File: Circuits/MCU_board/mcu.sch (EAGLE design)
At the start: 72 parts, among them IC1 RP111N331B-TR-FE, IC2 FT230XS, U1 TCA9548APWR, U2 USBLC6-2P6, U4 LSM9DS1, U5 STM32L452RECT6

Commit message: Finished first draft routing
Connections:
- net N$1 renamed D+
- net N$2 renamed D-
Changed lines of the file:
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@@
 </segment>
 </net>
-<net name="N$1" class="0">
+<net name="D+" class="0">
 <segment>
 <pinref part="CN1" gate="G$1" pin="D+"/>
@@
 <pinref part="U2" gate="G$1" pin="I/O1_2"/>
 <wire x1="205.74" y1="68.58" x2="195.58" y2="68.58" width="0.1524" layer="91"/>
+<label x="203.2" y="68.58" size="1.778" layer="95"/>
 </segment>
 </net>
-<net name="N$2" class="0">
+<net name="D-" class="0">
 <segment>
 <pinref part="CN1" gate="G$1" pin="D-"/>
@@
 <pinref part="U2" gate="G$1" pin="I/O2_2"/>
 <wire x1="205.74" y1="58.42" x2="195.58" y2="58.42" width="0.1524" layer="91"/>
+<label x="203.2" y="58.42" size="1.778" layer="95"/>
 </segment>
 </net>

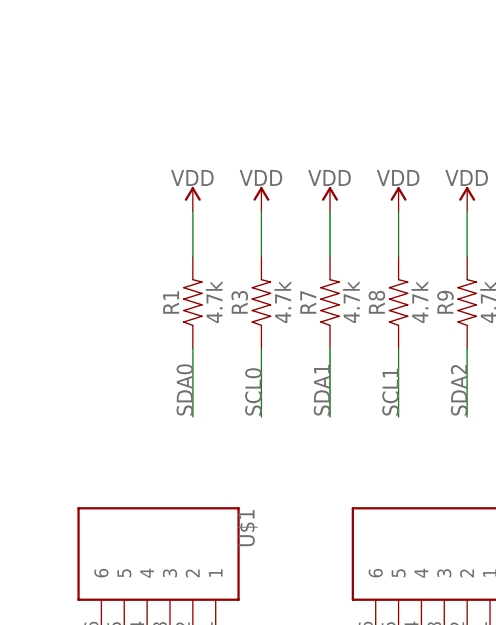
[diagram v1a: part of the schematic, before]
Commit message: Add pullups for MCU I2C lines
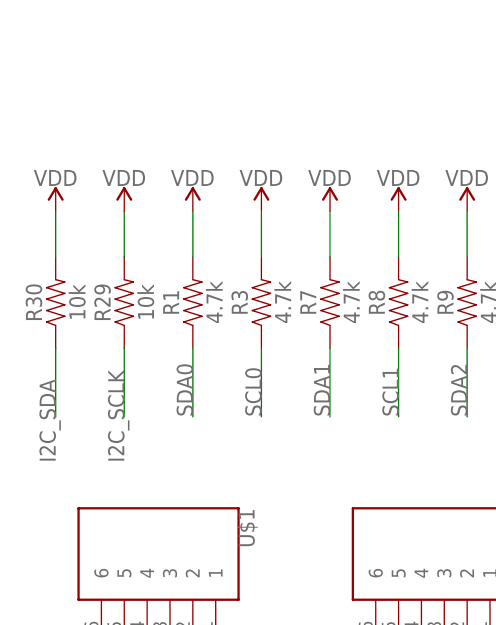
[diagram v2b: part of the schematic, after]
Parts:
- added R29, R30: 10k, SparkFun-Resistors:10KOHM-0603-1/10W-1%
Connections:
- net I2C_SCLK: now also R29.1
- net I2C_SDA: now also R30.1
- net VDD: now also R29.2, R30.2
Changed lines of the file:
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@@
 <?xml version="1.0" encoding="utf-8"?>
 <!DOCTYPE eagle SYSTEM "eagle.dtd">
-<eagle version="9.4.2">
+<eagle version="9.3.2">
 <drawing>
 <settings>
@@
 <part name="R25" library="SparkFun-Resistors" deviceset="10KOHM" device="-0603-1/10W-1%" value="10k"/>
 <part name="R26" library="SparkFun-Resistors" deviceset="10KOHM" device="-0603-1/10W-1%" value="10k"/>
+<part name="R29" library="SparkFun-Resistors" deviceset="10KOHM" device="-0603-1/10W-1%" value="10k"/>
+<part name="R30" library="SparkFun-Resistors" deviceset="10KOHM" device="-0603-1/10W-1%" value="10k"/>
+<part name="SUPPLY26" library="SparkFun-PowerSymbols" deviceset="VDD" device=""/>
+<part name="SUPPLY27" library="SparkFun-PowerSymbols" deviceset="VDD" device=""/>
 </parts>
 <sheets>
@@
 <attribute name="NAME" x="105.156" y="7.62" size="1.778" layer="95" font="vector" rot="R90" align="bottom-center"/>
 <attribute name="VALUE" x="108.204" y="7.62" size="1.778" layer="96" font="vector" rot="R90" align="top-center"/>
+</instance>
+<instance part="R29" gate="G$1" x="-215.9" y="119.38" smashed="yes" rot="R90">
+<attribute name="NAME" x="-217.424" y="119.38" size="1.778" layer="95" font="vector" rot="R90" align="bottom-center"/>
+<attribute name="VALUE" x="-214.376" y="119.38" size="1.778" layer="96" font="vector" rot="R90" align="top-center"/>
+</instance>
+<instance part="R30" gate="G$1" x="-223.52" y="119.38" smashed="yes" rot="R90">
+<attribute name="NAME" x="-225.044" y="119.38" size="1.778" layer="95" font="vector" rot="R90" align="bottom-center"/>
+<attribute name="VALUE" x="-221.996" y="119.38" size="1.778" layer="96" font="vector" rot="R90" align="top-center"/>
+</instance>
+<instance part="SUPPLY26" gate="VDD" x="-215.9" y="129.54" smashed="yes">
+<attribute name="VALUE" x="-215.9" y="132.334" size="1.778" layer="96" align="bottom-center"/>
+</instance>
+<instance part="SUPPLY27" gate="VDD" x="-223.52" y="129.54" smashed="yes">
+<attribute name="VALUE" x="-223.52" y="132.334" size="1.778" layer="96" align="bottom-center"/>
 </instance>
 </instances>
@@
 <label x="-96.52" y="63.5" size="1.778" layer="95" rot="R90"/>
 </segment>
+<segment>
+<pinref part="R29" gate="G$1" pin="2"/>
+<wire x1="-215.9" y1="124.46" x2="-215.9" y2="129.54" width="0.1524" layer="91"/>
+<pinref part="SUPPLY26" gate="VDD" pin="VDD"/>
+</segment>
+<segment>
+<pinref part="R30" gate="G$1" pin="2"/>
+<wire x1="-223.52" y1="124.46" x2="-223.52" y2="129.54" width="0.1524" layer="91"/>
+<pinref part="SUPPLY27" gate="VDD" pin="VDD"/>
+</segment>
 </net>
 <net name="USB_D-" class="0">
@@
 <label x="-35.56" y="76.2" size="1.778" layer="95"/>
 </segment>
+<segment>
+<pinref part="R30" gate="G$1" pin="1"/>
+<wire x1="-223.52" y1="114.3" x2="-223.52" y2="106.68" width="0.1524" layer="91"/>
+<label x="-223.52" y="101.6" size="1.778" layer="95" rot="R90"/>
+</segment>
 </net>
 <net name="I2C_SCLK" class="0">
@@
 <label x="-35.56" y="78.74" size="1.778" layer="95"/>
 </segment>
+<segment>
+<pinref part="R29" gate="G$1" pin="1"/>
+<wire x1="-215.9" y1="114.3" x2="-215.9" y2="106.68" width="0.1524" layer="91"/>
+<label x="-215.9" y="101.6" size="1.778" layer="95" rot="R90"/>
+</segment>
 </net>

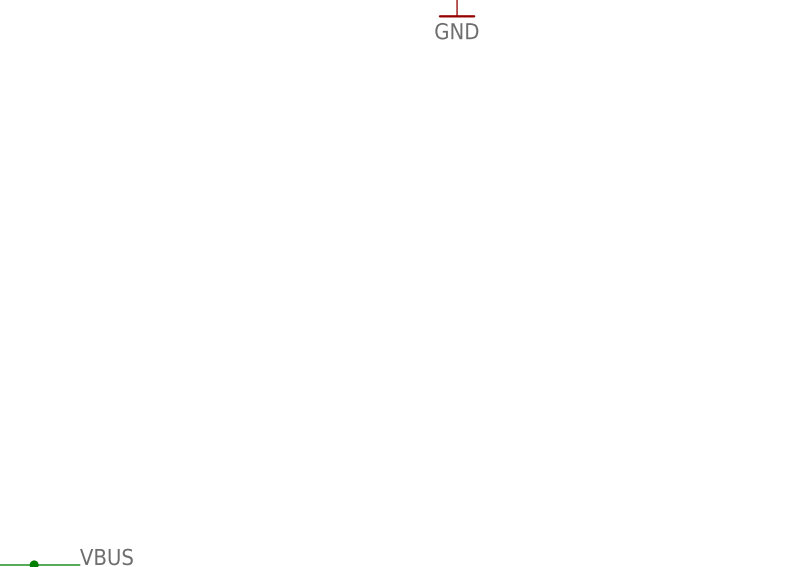
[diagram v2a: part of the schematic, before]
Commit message: Moved FTDI and re-routed, Added VCCIO plane and shrunk VDD plane, Added VDD and GND Test Point
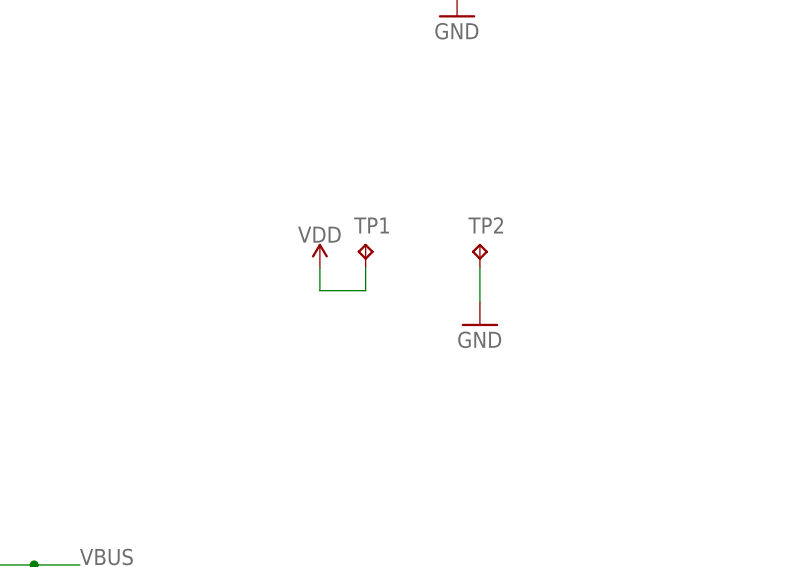
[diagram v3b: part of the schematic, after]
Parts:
- added TP1, TP2: TPB2,54, testpad:TPB2,54
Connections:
- net GND: now also TP2.TP
- net VDD: now also TP1.TP
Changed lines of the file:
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@@
 <?xml version="1.0" encoding="utf-8"?>
 <!DOCTYPE eagle SYSTEM "eagle.dtd">
-<eagle version="9.3.2">
+<eagle version="9.4.2">
 <drawing>
 <settings>
@@
 <setting verticaltext="up"/>
 </settings>
-<grid distance="0.1" unitdist="inch" unit="inch" style="lines" multiple="1" display="no" altdistance="0.01" altunitdist="inch" altunit="inch"/>
+<grid distance="0.1" unitdist="inch" unit="inch" style="lines" multiple="1" display="yes" altdistance="0.01" altunitdist="inch" altunit="inch"/>
 <layers>
 <layer number="1" name="Top" color="4" fill="1" visible="no" active="no"/>
@@
 <part name="SUPPLY26" library="SparkFun-PowerSymbols" deviceset="VDD" device=""/>
 <part name="SUPPLY27" library="SparkFun-PowerSymbols" deviceset="VDD" device=""/>
+<part name="TP1" library="testpad" library_urn="urn:adsk.eagle:library:385" deviceset="TP" device="B2,54" package3d_urn="urn:adsk.eagle:package:27948/1"/>
+<part name="TP2" library="testpad" library_urn="urn:adsk.eagle:library:385" deviceset="TP" device="B2,54" package3d_urn="urn:adsk.eagle:package:27948/1"/>
+<part name="SUPPLY28" library="SparkFun-PowerSymbols" deviceset="VDD" device=""/>
+<part name="GND31" library="supply1" library_urn="urn:adsk.eagle:library:371" deviceset="GND" device=""/>
 </parts>
 <sheets>
@@
 <instance part="SUPPLY27" gate="VDD" x="-223.52" y="129.54" smashed="yes">
 <attribute name="VALUE" x="-223.52" y="132.334" size="1.778" layer="96" align="bottom-center"/>
+</instance>
+<instance part="TP1" gate="G$1" x="190.5" y="10.16" smashed="yes">
+<attribute name="NAME" x="189.23" y="11.43" size="1.778" layer="95"/>
+<attribute name="TP_SIGNAL_NAME" x="191.77" y="8.89" size="1.778" layer="97"/>
+</instance>
+<instance part="TP2" gate="G$1" x="203.2" y="10.16" smashed="yes">
+<attribute name="NAME" x="201.93" y="11.43" size="1.778" layer="95"/>
+<attribute name="TP_SIGNAL_NAME" x="204.47" y="8.89" size="1.778" layer="97"/>
+</instance>
+<instance part="SUPPLY28" gate="VDD" x="185.42" y="7.62" smashed="yes">
+<attribute name="VALUE" x="185.42" y="10.414" size="1.778" layer="96" align="bottom-center"/>
+</instance>
+<instance part="GND31" gate="1" x="203.2" y="1.27" smashed="yes">
+<attribute name="VALUE" x="200.66" y="-1.27" size="1.778" layer="96"/>
 </instance>
 </instances>
@@
 <wire x1="-93.98" y1="81.28" x2="-93.98" y2="63.5" width="0.1524" layer="91"/>
 <label x="-93.98" y="63.5" size="1.778" layer="95" rot="R90"/>
+</segment>
+<segment>
+<pinref part="TP2" gate="G$1" pin="TP"/>
+<pinref part="GND31" gate="1" pin="GND"/>
+<wire x1="203.2" y1="7.62" x2="203.2" y2="3.81" width="0.1524" layer="91"/>
 </segment>
 </net>
@@
 <pinref part="SUPPLY27" gate="VDD" pin="VDD"/>
 </segment>
+<segment>
+<pinref part="SUPPLY28" gate="VDD" pin="VDD"/>
+<wire x1="185.42" y1="7.62" x2="185.42" y2="5.08" width="0.1524" layer="91"/>
+<pinref part="TP1" gate="G$1" pin="TP"/>
+<wire x1="185.42" y1="5.08" x2="190.5" y2="5.08" width="0.1524" layer="91"/>
+<wire x1="190.5" y1="5.08" x2="190.5" y2="7.62" width="0.1524" layer="91"/>
+</segment>
 </net>

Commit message: Revert "Moved FTDI and re-routed, Added VCCIO plane and shrunk VDD plane, Added VDD and GND Test Point"
This reverts commit a39282d0876712c586134e04e0ec14b12e122efb.
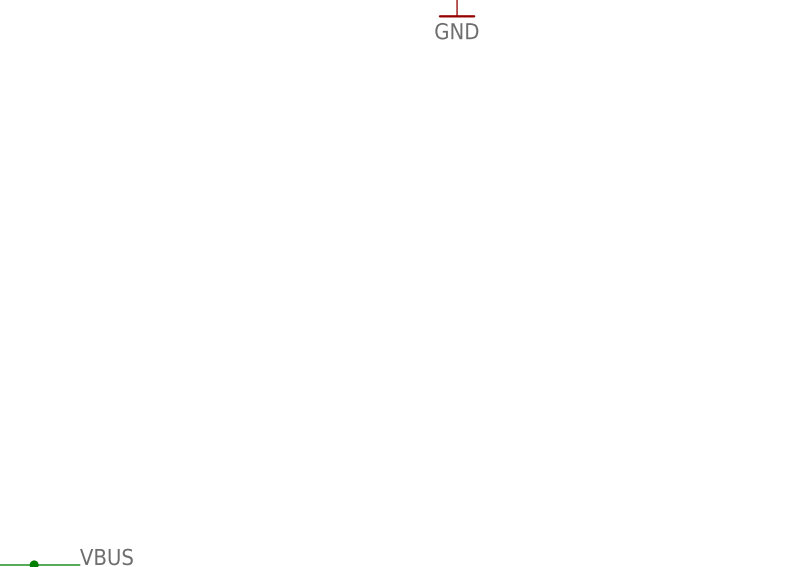
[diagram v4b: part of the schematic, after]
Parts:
- removed TP1, TP2: TPB2,54, testpad:TPB2,54
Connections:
- net GND: no longer TP2.TP
- net VDD: no longer TP1.TP
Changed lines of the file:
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@@
 <?xml version="1.0" encoding="utf-8"?>
 <!DOCTYPE eagle SYSTEM "eagle.dtd">
-<eagle version="9.4.2">
+<eagle version="9.3.2">
 <drawing>
 <settings>
@@
 <setting verticaltext="up"/>
 </settings>
-<grid distance="0.1" unitdist="inch" unit="inch" style="lines" multiple="1" display="yes" altdistance="0.01" altunitdist="inch" altunit="inch"/>
+<grid distance="0.1" unitdist="inch" unit="inch" style="lines" multiple="1" display="no" altdistance="0.01" altunitdist="inch" altunit="inch"/>
 <layers>
 <layer number="1" name="Top" color="4" fill="1" visible="no" active="no"/>
@@
 <part name="SUPPLY26" library="SparkFun-PowerSymbols" deviceset="VDD" device=""/>
 <part name="SUPPLY27" library="SparkFun-PowerSymbols" deviceset="VDD" device=""/>
-<part name="TP1" library="testpad" library_urn="urn:adsk.eagle:library:385" deviceset="TP" device="B2,54" package3d_urn="urn:adsk.eagle:package:27948/1"/>
-<part name="TP2" library="testpad" library_urn="urn:adsk.eagle:library:385" deviceset="TP" device="B2,54" package3d_urn="urn:adsk.eagle:package:27948/1"/>
-<part name="SUPPLY28" library="SparkFun-PowerSymbols" deviceset="VDD" device=""/>
-<part name="GND31" library="supply1" library_urn="urn:adsk.eagle:library:371" deviceset="GND" device=""/>
 </parts>
 <sheets>
@@
 <instance part="SUPPLY27" gate="VDD" x="-223.52" y="129.54" smashed="yes">
 <attribute name="VALUE" x="-223.52" y="132.334" size="1.778" layer="96" align="bottom-center"/>
-</instance>
-<instance part="TP1" gate="G$1" x="190.5" y="10.16" smashed="yes">
-<attribute name="NAME" x="189.23" y="11.43" size="1.778" layer="95"/>
-<attribute name="TP_SIGNAL_NAME" x="191.77" y="8.89" size="1.778" layer="97"/>
-</instance>
-<instance part="TP2" gate="G$1" x="203.2" y="10.16" smashed="yes">
-<attribute name="NAME" x="201.93" y="11.43" size="1.778" layer="95"/>
-<attribute name="TP_SIGNAL_NAME" x="204.47" y="8.89" size="1.778" layer="97"/>
-</instance>
-<instance part="SUPPLY28" gate="VDD" x="185.42" y="7.62" smashed="yes">
-<attribute name="VALUE" x="185.42" y="10.414" size="1.778" layer="96" align="bottom-center"/>
-</instance>
-<instance part="GND31" gate="1" x="203.2" y="1.27" smashed="yes">
-<attribute name="VALUE" x="200.66" y="-1.27" size="1.778" layer="96"/>
 </instance>
 </instances>
@@
 <wire x1="-93.98" y1="81.28" x2="-93.98" y2="63.5" width="0.1524" layer="91"/>
 <label x="-93.98" y="63.5" size="1.778" layer="95" rot="R90"/>
-</segment>
-<segment>
-<pinref part="TP2" gate="G$1" pin="TP"/>
-<pinref part="GND31" gate="1" pin="GND"/>
-<wire x1="203.2" y1="7.62" x2="203.2" y2="3.81" width="0.1524" layer="91"/>
 </segment>
 </net>
@@
 <pinref part="SUPPLY27" gate="VDD" pin="VDD"/>
 </segment>
-<segment>
-<pinref part="SUPPLY28" gate="VDD" pin="VDD"/>
-<wire x1="185.42" y1="7.62" x2="185.42" y2="5.08" width="0.1524" layer="91"/>
-<pinref part="TP1" gate="G$1" pin="TP"/>
-<wire x1="185.42" y1="5.08" x2="190.5" y2="5.08" width="0.1524" layer="91"/>
-<wire x1="190.5" y1="5.08" x2="190.5" y2="7.62" width="0.1524" layer="91"/>
-</segment>
 </net>
